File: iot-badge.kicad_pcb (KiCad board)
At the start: 2 copper layers, 100 x 70 mm, 14 parts, among them J1 USB_C_Receptacle_USB2.0, J11 Conn_01x01_Male, J12 Conn_01x01_Male, SW1 SW_Push, SW2 SW_Push, SW3 SW_Push, SW4 SW_Push, SW5 SW_Push, SW6 SW_Push, U1 ESP32-WROOM-32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

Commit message: started readme
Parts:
- BT1: footprint Battery:BatteryHolder_Keystone_3009_1x2450 -> Battery:BatteryHolder_Keystone_1057_1x2032
- moved BT1 29.1 mm to (149.9, 96.5), turned to 0 degrees

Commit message: pcb antenna finished
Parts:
- added AE1: Antenna, RF_PCB_Antenna:Micrel_Heli_2, F.Cu at (152.4, 63.5)
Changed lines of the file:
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@@
   (net 74 "unconnected-(J1-PadB8)")
   (net 75 "unconnected-(J1-PadS1)")
+  (net 76 "unconnected-(AE1-Pad1)")
   (footprint "Symbol:OSHW-Symbol_6.7x6mm_SilkScreen" (layer "F.Cu")
     (at 104.71912 121.73712 90)
@@
     (fp_line (start -11.308824 -3.917435) (end -11.035498 -4.091883) (layer "Edge.Cuts") (width 0.1))
     (fp_arc (start 14.7 3.282793) (mid 14.582845 3.56564) (end 14.3 3.682793) (layer "Edge.Cuts") (width 0.1))
-    (fp_arc (start 14.3 1.68505) (mid 14.582825 1.80221) (end 14.7 2.08505) (layer "Edge.Cuts") (width 0.1))
+    (fp_arc (start 14.3 1.68505) (mid 14.58286 1.802204) (end 14.7 2.08505) (layer "Edge.Cuts") (width 0.1))
     (fp_arc (start -14.7 -3.285) (mid -14.582843 -3.567843) (end -14.3 -3.685) (layer "Edge.Cuts") (width 0.1))
     (fp_arc (start -14.3 -1.68505) (mid -14.582843 -1.802207) (end -14.7 -2.08505) (layer "Edge.Cuts") (width 0.1))
@@
     (fp_line (start 12.25 -3.95) (end 15 -3.95) (layer "F.CrtYd") (width 0.05))
     (fp_arc (start -10.9 -4.65) (mid -11.492594 -4.141075) (end -12.25 -3.95) (layer "F.CrtYd") (width 0.05))
-    (fp_arc (start 12.25 -3.95) (mid 11.492602 -4.141084) (end 10.9 -4.65) (layer "F.CrtYd") (width 0.05))
+    (fp_arc (start 12.25 -3.95) (mid 11.492593 -4.141077) (end 10.9 -4.65) (layer "F.CrtYd") (width 0.05))
     (fp_arc (start -10.9 -4.65) (mid 0 -11.772188) (end 10.9 -4.65) (layer "F.CrtYd") (width 0.05))
-    (fp_arc (start 10.9 4.65) (mid 11.492593 4.141066) (end 12.25 3.95) (layer "F.CrtYd") (width 0.05))
+    (fp_arc (start 10.9 4.65) (mid 11.492591 4.141073) (end 12.25 3.95) (layer "F.CrtYd") (width 0.05))
     (fp_arc (start -12.25 3.95) (mid -11.492594 4.141075) (end -10.9 4.65) (layer "F.CrtYd") (width 0.05))
     (fp_arc (start 10.9 4.65) (mid 0 11.7722) (end -10.9 4.65) (layer "F.CrtYd") (width 0.05))
@@
     )
   )
+  (footprint "RF_PCB_Antenna:Micrel_Heli_2" (layer "F.Cu")
+    (at 152.4 63.5)
+    (descr "PCB ANTENNA 300-450 MHz Micrel Heli 2 AN 52")
+    (property "Sheetfile" "iot-badge.kicad_sch")
+    (property "Sheetname" "")
+    (attr smd)
+    (fp_text reference "AE1" (at 0 10.16 unlocked) (layer "F.SilkS")
+      (effects (font (size 1 1) (thickness 0.15)))
+    )
+    (fp_text value "Antenna" (at 0 7.62 unlocked) (layer "F.Fab")
+      (effects (font (size 1 1) (thickness 0.15)))
+    )
+    (fp_text user "${REFERENCE}" (at 0 10.16 unlocked) (layer "F.Fab")
+      (effects (font (size 1 1) (thickness 0.15)))
+    )
+    (fp_line (start 3.556 2.032) (end 4.572 -2.032) (layer "F.Cu") (width 1.016))
+    (fp_line (start -4.572 2.032) (end -3.556 -2.032) (layer "F.Cu") (width 1.016))
+    (fp_line (start -2.54 2.032) (end -1.524 -2.032) (layer "F.Cu") (width 1.016))
+    (fp_line (start 9.652 2.032) (end 10.668 -2.032) (layer "F.Cu") (width 1.016))
+    (fp_line (start 11.684 2.032) (end 12.7 -2.032) (layer "F.Cu") (width 1.016))
+    (fp_line (start -10.668 2.032) (end -9.652 -2.032) (layer "F.Cu") (width 1.016))
+    (fp_line (start -12.7 2.032) (end -11.684 -2.032) (layer "F.Cu") (width 1.016))
+    (fp_line (start -0.508 2.032) (end 0.508 -2.032) (layer "F.Cu") (width 1.016))
+    (fp_line (start 1.524 2.032) (end 2.54 -2.032) (layer "F.Cu") (width 1.016))
+    (fp_line (start -8.636 2.032) (end -7.62 -2.032) (layer "F.Cu") (width 1.016))
+    (fp_line (start 7.62 2.032) (end 8.636 -2.032) (layer "F.Cu") (width 1.016))
+    (fp_line (start 5.588 2.032) (end 6.604 -2.032) (layer "F.Cu") (width 1.016))
+    (fp_line (start 13.716 2.032) (end 14.732 -2.032) (layer "F.Cu") (width 1.016))
+    (fp_line (start -16.8 4.5966) (end -16.8 5.8) (layer "F.Cu") (width 0.2))
+    (fp_line (start -14.732 2.032) (end -13.716 -2.032) (layer "F.Cu") (width 1.016))
+    (fp_line (start -6.604 2.032) (end -5.588 -2.032) (layer "F.Cu") (width 1.016))
+    (fp_line (start -16.8 4.5966) (end -15.748 -2.032) (layer "F.Cu") (width 1.016))
+    (fp_line (start -6.604 2.032) (end -7.62 -2.032) (layer "B.Cu") (width 1.016))
+    (fp_line (start 1.524 2.032) (end 0.508 -2.032) (layer "B.Cu") (width 1.016))
+    (fp_line (start 9.652 2.032) (end 8.636 -2.032) (layer "B.Cu") (width 1.016))
+    (fp_line (start -0.508 2.032) (end -1.524 -2.032) (layer "B.Cu") (width 1.016))
+    (fp_line (start 15.748 2.032) (end 14.732 -2.032) (layer "B.Cu") (width 1.016))
+    (fp_line (start 11.684 2.032) (end 10.668 -2.032) (layer "B.Cu") (width 1.016))
+    (fp_line (start -12.7 2.032) (end -13.716 -2.032) (layer "B.Cu") (width 1.016))
+    (fp_line (start 3.556 2.032) (end 2.54 -2.032) (layer "B.Cu") (width 1.016))
+    (fp_line (start -14.732 2.032) (end -15.748 -2.032) (layer "B.Cu") (width 1.016))
+    (fp_line (start -10.668 2.032) (end -11.684 -2.032) (layer "B.Cu") (width 1.016))
+    (fp_line (start 5.588 2.032) (end 4.572 -2.032) (layer "B.Cu") (width 1.016))
+    (fp_line (start 7.62 2.032) (end 6.604 -2.032) (layer "B.Cu") (width 1.016))
+    (fp_line (start -4.572 2.032) (end -5.588 -2.032) (layer "B.Cu") (width 1.016))
+    (fp_line (start 13.716 2.032) (end 12.7 -2.032) (layer "B.Cu") (width 1.016))
+    (fp_line (start -2.54 2.032) (end -3.556 -2.032) (layer "B.Cu") (width 1.016))
+    (fp_line (start -8.636 2.032) (end -9.652 -2.032) (layer "B.Cu") (width 1.016))
+    (fp_line (start 21.3 5.1892) (end -11.24 5.1892) (layer "F.CrtYd") (width 0.05))
+    (fp_line (start -17.78 6.95) (end -22.5 6.95) (layer "F.CrtYd") (width 0.05))
+    (fp_line (start 21.3 -7.58) (end 21.3 5.1892) (layer "F.CrtYd") (width 0.05))
+    (fp_line (start -11.24 6.95) (end -11.24 5.1892) (layer "F.CrtYd") (width 0.05))
+    (fp_line (start -11.24 6.95) (end -17.78 6.95) (layer "F.CrtYd") (width 0.05))
+    (fp_line (start -22.5 -7.58) (end -22.5 6.95) (layer "F.CrtYd") (width 0.05))
+    (fp_line (start -22.5 -7.58) (end 21.3 -7.58) (layer "F.CrtYd") (width 0.05))
+    (pad "" thru_hole circle (at -5.588 -2.032) (size 1 1) (drill 0.508) (layers *.Cu *.Mask))
+    (pad "" thru_hole circle (at -6.604 2.032) (size 1 1) (drill 0.508) (layers *.Cu *.Mask))
+    (pad "" thru_hole circle (at 7.62 2.032) (size 1 1) (drill 0.508) (layers *.Cu *.Mask))
+    (pad "" thru_hole circle (at 1.524 2.032) (size 1 1) (drill 0.508) (layers *.Cu *.Mask))
+    (pad "" thru_hole circle (at 12.7 -2.032) (size 1 1) (drill 0.508) (layers *.Cu *.Mask))
+    (pad "" thru_hole circle (at -3.556 -2.032) (size 1 1) (drill 0.508) (layers *.Cu *.Mask))
+    (pad "" thru_hole circle (at 5.588 2.032) (size 1 1) (drill 0.508) (layers *.Cu *.Mask))
+    (pad "" thru_hole circle (at -0.508 2.032) (size 1 1) (drill 0.508) (layers *.Cu *.Mask))
+    (pad "" thru_hole circle (at -1.524 -2.032) (size 1 1) (drill 0.508) (layers *.Cu *.Mask))
+    (pad "" thru_hole circle (at -10.668 2.032) (size 1 1) (drill 0.508) (layers *.Cu *.Mask))
+    (pad "" thru_hole circle (at 3.556 2.032) (size 1 1) (drill 0.508) (layers *.Cu *.Mask))
+    (pad "" thru_hole circle (at -8.636 2.032) (size 1 1) (drill 0.508) (layers *.Cu *.Mask))
+    (pad "" thru_hole circle (at 13.716 2.032) (size 1 1) (drill 0.508) (layers *.Cu *.Mask))
+    (pad "" thru_hole circle (at 6.604 -2.032) (size 1 1) (drill 0.508) (layers *.Cu *.Mask))
+    (pad "" thru_hole circle (at 2.54 -2.032) (size 1 1) (drill 0.508) (layers *.Cu *.Mask))
+    (pad "" thru_hole circle (at 15.748 2.032) (size 1 1) (drill 0.508) (layers *.Cu *.Mask))
+    (pad "" thru_hole circle (at 0.508 -2.032) (size 1 1) (drill 0.508) (layers *.Cu *.Mask))
+    (pad "" thru_hole circle (at 4.572 -2.032) (size 1 1) (drill 0.508) (layers *.Cu *.Mask))
+    (pad "" thru_hole circle (at -4.572 2.032) (size 1 1) (drill 0.508) (layers *.Cu *.Mask))
+    (pad "" thru_hole circle (at -9.652 -2.032) (size 1 1) (drill 0.508) (layers *.Cu *.Mask))
+    (pad "" thru_hole circle (at 8.636 -2.032) (size 1 1) (drill 0.508) (layers *.Cu *.Mask))
+    (pad "" thru_hole circle (at -13.716 -2.032) (size 1 1) (drill 0.508) (layers *.Cu *.Mask))
+    (pad "" thru_hole circle (at -7.62 -2.032) (size 1 1) (drill 0.508) (layers *.Cu *.Mask))
+    (pad "" thru_hole circle (at -11.684 -2.032) (size 1 1) (drill 0.508) (layers *.Cu *.Mask))
+    (pad "" thru_hole circle (at -12.7 2.032) (size 1 1) (drill 0.508) (layers *.Cu *.Mask))
+    (pad "" thru_hole circle (at -14.732 2.032) (size 1 1) (drill 0.508) (layers *.Cu *.Mask))
+    (pad "" thru_hole circle (at -15.748 -2.032) (size 1 1) (drill 0.508) (layers *.Cu *.Mask))
+    (pad "" thru_hole circle (at 14.732 -2.032) (size 1 1) (drill 0.508) (layers *.Cu *.Mask))
+    (pad "" thru_hole circle (at -2.54 2.032) (size 1 1) (drill 0.508) (layers *.Cu *.Mask))
+    (pad "" thru_hole circle (at 9.652 2.032) (size 1 1) (drill 0.508) (layers *.Cu *.Mask))
+    (pad "" thru_hole circle (at 10.668 -2.032) (size 1 1) (drill 0.508) (layers *.Cu *.Mask))
+    (pad "" thru_hole circle (at 11.684 2.032) (size 1 1) (drill 0.508) (layers *.Cu *.Mask))
+    (pad "1" smd roundrect (at -16.8 6) (size 1.2 1.4) (layers "F.Cu" "F.Paste" "F.Mask") (roundrect_rratio 0.2083333333)
+      (net 76 "unconnected-(AE1-Pad1)") (pinfunction "A") (pintype "input"))
+    (zone (net 0) (net_name "") (layers F&B.Cu "F.CrtYd") (hatch edge 0.508)
+      (connect_pads (clearance 0))
+      (min_thickness 0.254)
+      (keepout (tracks not_allowed) (vias not_allowed) (pads not_allowed) (copperpour not_allowed) (footprints not_allowed))
+      (fill (thermal_gap 0.508) (thermal_bridge_width 0.508))
+      (polygon
+        (pts
+          (xy 173.7 68.6892)
+          (xy 141.16 68.6892)
+          (xy 141.16 70.45)
+          (xy 137.89 70.45)
+          (xy 137.16 68.58)
+          (xy 135 69.05)
+          (xy 134.62 70.45)
+          (xy 129.9 70.45)
+          (xy 129.9 55.92)
+          (xy 173.7 55.92)
+        )
+      )
+    )
+  )

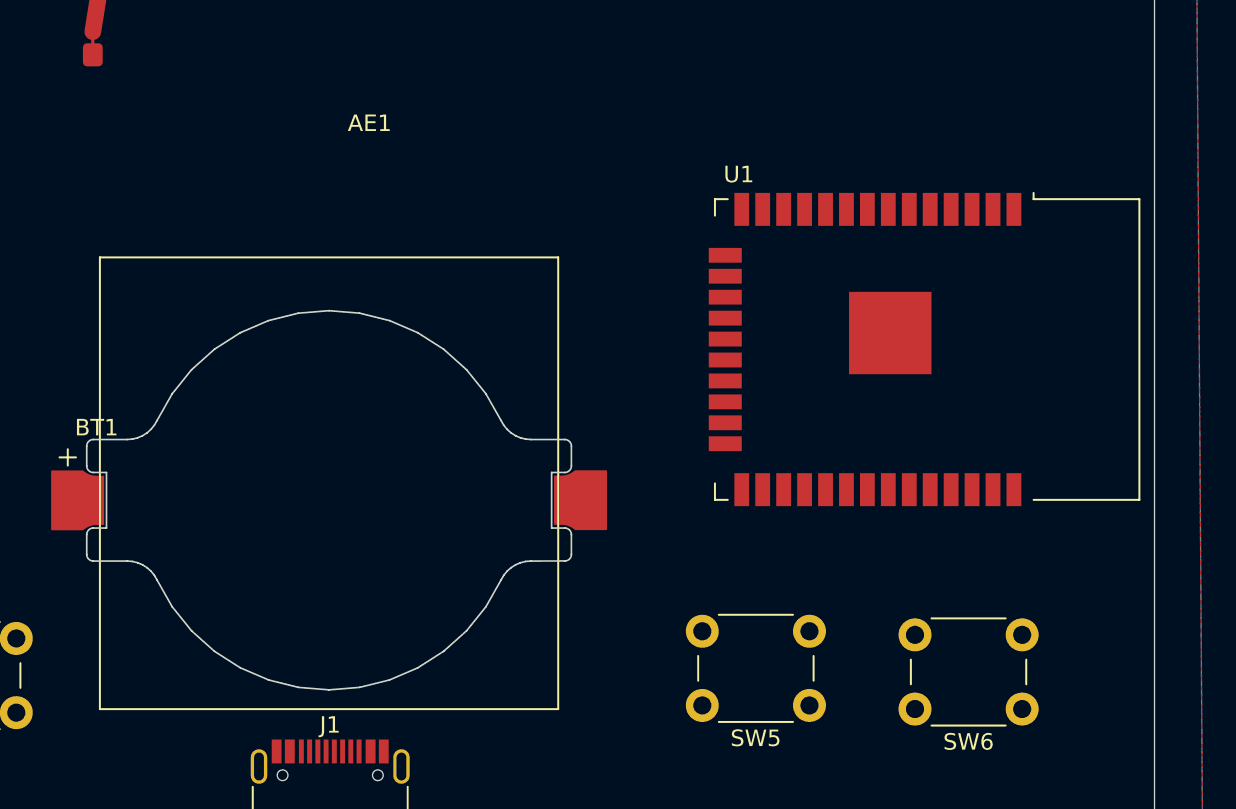
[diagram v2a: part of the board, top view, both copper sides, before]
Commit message: i2c display footprint started
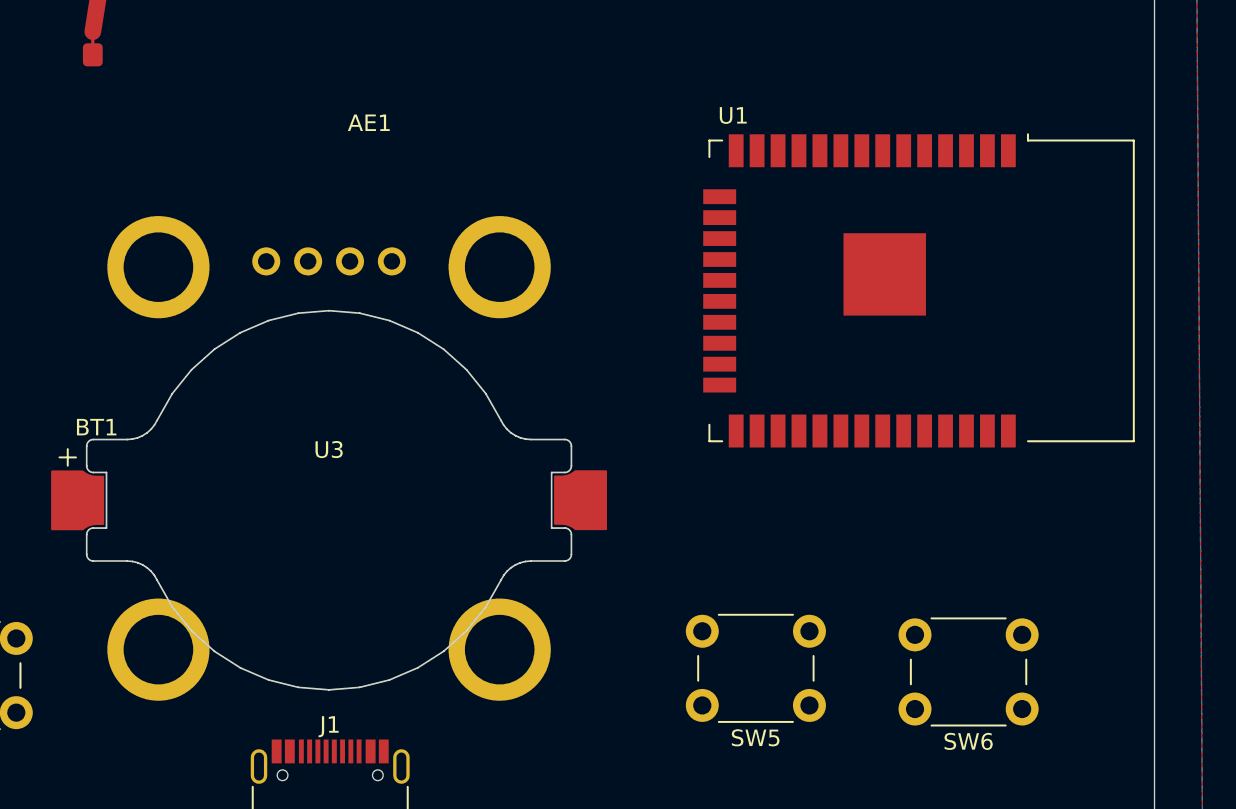
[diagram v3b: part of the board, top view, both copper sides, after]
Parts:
- added U3: DISPLAY_SSD1306_128x64_I2C, Display_PCB:DISPLAY_SSD1306_128x64_I2C_0.96inch, F.Cu at (149.9, 94.0)
- moved U1 3.57 mm to (182.9, 83.8)
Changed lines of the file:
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@@
   (net 75 "unconnected-(J1-PadS1)")
   (net 76 "unconnected-(AE1-Pad1)")
+  (net 77 "unconnected-(U3-Pad1)")
+  (net 78 "unconnected-(U3-Pad2)")
+  (net 79 "unconnected-(U3-Pad3)")
+  (net 80 "unconnected-(U3-Pad4)")
   (footprint "Symbol:OSHW-Symbol_6.7x6mm_SilkScreen" (layer "F.Cu")
     (at 104.71912 121.73712 90)
@@
   )
   (footprint "RF_Module:ESP32-WROOM-32" (layer "F.Cu")
-    (at 183.218 87.376 -90)
+    (at 182.88 83.82 -90)
     (descr "Single 2.4 GHz Wi-Fi and Bluetooth combo chip https://www.espressif.com/sites/default/files/documentation/esp32-wroom-32_datasheet_en.pdf")
     (tags "Single 2.4 GHz Wi-Fi and Bluetooth combo  chip")
@@
       (polygon
         (pts
-          (xy 193.188 73.376)
-          (xy 193.188 101.376)
-          (xy 203.968 101.376)
-          (xy 203.968 73.376)
+          (xy 192.85 69.82)
+          (xy 192.85 97.82)
+          (xy 203.63 97.82)
+          (xy 203.63 69.82)
         )
       )
@@
     (fp_line (start -11.308824 -3.917435) (end -11.035498 -4.091883) (layer "Edge.Cuts") (width 0.1))
     (fp_arc (start 14.7 3.282793) (mid 14.582845 3.56564) (end 14.3 3.682793) (layer "Edge.Cuts") (width 0.1))
-    (fp_arc (start 14.3 1.68505) (mid 14.58286 1.802204) (end 14.7 2.08505) (layer "Edge.Cuts") (width 0.1))
+    (fp_arc (start 14.3 1.68505) (mid 14.582825 1.80221) (end 14.7 2.08505) (layer "Edge.Cuts") (width 0.1))
     (fp_arc (start -14.7 -3.285) (mid -14.582843 -3.567843) (end -14.3 -3.685) (layer "Edge.Cuts") (width 0.1))
     (fp_arc (start -14.3 -1.68505) (mid -14.582843 -1.802207) (end -14.7 -2.08505) (layer "Edge.Cuts") (width 0.1))
@@
     (fp_line (start 12.25 -3.95) (end 15 -3.95) (layer "F.CrtYd") (width 0.05))
     (fp_arc (start -10.9 -4.65) (mid -11.492594 -4.141075) (end -12.25 -3.95) (layer "F.CrtYd") (width 0.05))
-    (fp_arc (start 12.25 -3.95) (mid 11.492593 -4.141077) (end 10.9 -4.65) (layer "F.CrtYd") (width 0.05))
+    (fp_arc (start 12.25 -3.95) (mid 11.492602 -4.141084) (end 10.9 -4.65) (layer "F.CrtYd") (width 0.05))
     (fp_arc (start -10.9 -4.65) (mid 0 -11.772188) (end 10.9 -4.65) (layer "F.CrtYd") (width 0.05))
-    (fp_arc (start 10.9 4.65) (mid 11.492591 4.141073) (end 12.25 3.95) (layer "F.CrtYd") (width 0.05))
+    (fp_arc (start 10.9 4.65) (mid 11.492593 4.141072) (end 12.25 3.95) (layer "F.CrtYd") (width 0.05))
     (fp_arc (start -12.25 3.95) (mid -11.492594 4.141075) (end -10.9 4.65) (layer "F.CrtYd") (width 0.05))
     (fp_arc (start 10.9 4.65) (mid 0 11.7722) (end -10.9 4.65) (layer "F.CrtYd") (width 0.05))
@@
       (rotate (xyz 0 0 0))
     )
+  )
+  (footprint "Display_PCB:DISPLAY_SSD1306_128x64_I2C_0.96inch" (layer "F.Cu")
+    (at 149.93 93.98)
+    (property "Sheetfile" "iot-badge.kicad_sch")
+    (property "Sheetname" "")
+    (attr through_hole)
+    (fp_text reference "U3" (at 0 -0.5 unlocked) (layer "F.SilkS")
+      (effects (font (size 1 1) (thickness 0.15)))
+    )
+    (fp_text value "DISPLAY_SSD1306_128x64_I2C" (at 0 1 unlocked) (layer "F.Fab")
+      (effects (font (size 1 1) (thickness 0.15)))
+    )
+    (fp_text user "${REFERENCE}" (at 0 2.5 unlocked) (layer "F.Fab")
+      (effects (font (size 1 1) (thickness 0.15)))
+    )
+    (pad "" thru_hole circle (at 10.35 11.6) (size 6.2 6.2) (drill 4.22) (layers *.Cu *.Mask))
+    (pad "" thru_hole circle (at 10.35 -11.6) (size 6.2 6.2) (drill 4.22) (layers *.Cu *.Mask))
+    (pad "" thru_hole circle (at -10.35 -11.6) (size 6.2 6.2) (drill 4.22) (layers *.Cu *.Mask))
+    (pad "" thru_hole circle (at -10.35 11.6) (size 6.2 6.2) (drill 4.22) (layers *.Cu *.Mask))
+    (pad "1" thru_hole circle (at -3.81 -11.95) (size 1.7 1.7) (drill 1) (layers *.Cu *.Mask)
+      (net 77 "unconnected-(U3-Pad1)") (pinfunction "GND") (pintype "input"))
+    (pad "2" thru_hole circle (at -1.27 -11.95) (size 1.7 1.7) (drill 1) (layers *.Cu *.Mask)
+      (net 78 "unconnected-(U3-Pad2)") (pinfunction "VCC") (pintype "input"))
+    (pad "3" thru_hole circle (at 1.27 -11.95) (size 1.7 1.7) (drill 1) (layers *.Cu *.Mask)
+      (net 79 "unconnected-(U3-Pad3)") (pinfunction "SCL") (pintype "input"))
+    (pad "4" thru_hole circle (at 3.81 -11.95) (size 1.7 1.7) (drill 1) (layers *.Cu *.Mask)
+      (net 80 "unconnected-(U3-Pad4)") (pinfunction "SDA") (pintype "input"))
   )
   (footprint "Button_Switch_THT:SW_PUSH_6mm" (layer "F.Cu")
@@
       ) (layer "B.Cu") (width 0.01) (fill solid))
   )
-  (gr_rect (start 163.83 109.188) (end 136.03 81.788) (layer "F.SilkS") (width 0.12) (fill none))
   (gr_line (start 100 50) (end 200 50) (layer "Edge.Cuts") (width 0.05))
   (gr_line (start 200 50) (end 200 120) (layer "Edge.Cuts") (width 0.05))
